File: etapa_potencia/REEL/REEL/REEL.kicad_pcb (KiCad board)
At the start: 2 copper layers, 91.4 x 50.8 mm, 39 parts, among them J1 Conn_display2, J2 Conn_display_2, J3 Conn_teclado, J4 Conn_audio, J5 USB_B_Mini, SW1 SW_Push, SW2 SW_Reed, SW4 BW, SW5 FW, U2 ESP32-WROOM-32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

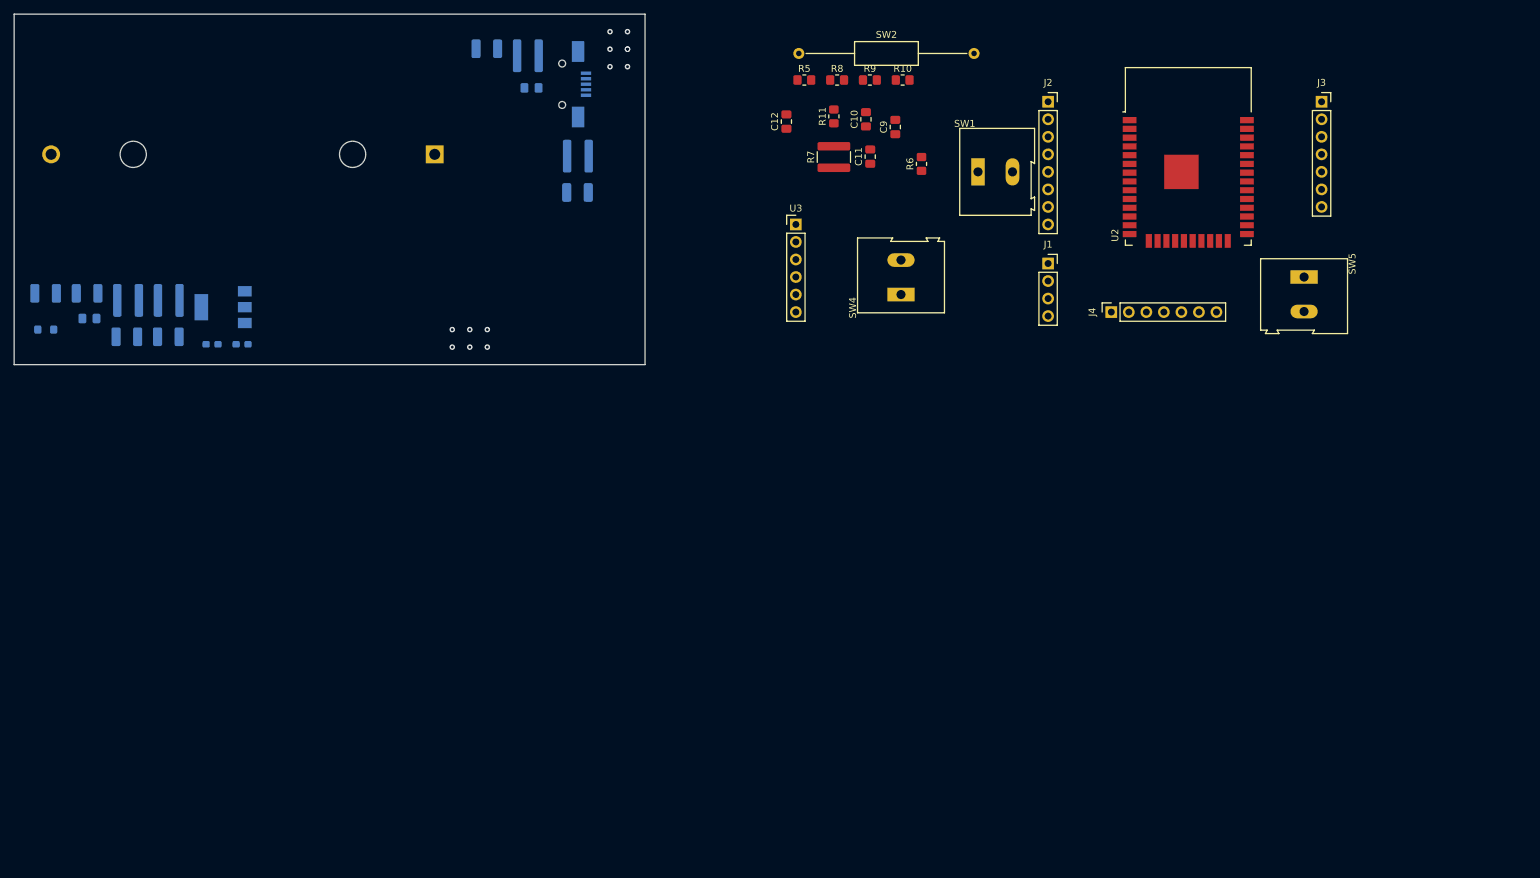
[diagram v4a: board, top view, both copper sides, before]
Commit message: Cambios en diagrama, separacion tierras, y capacitores
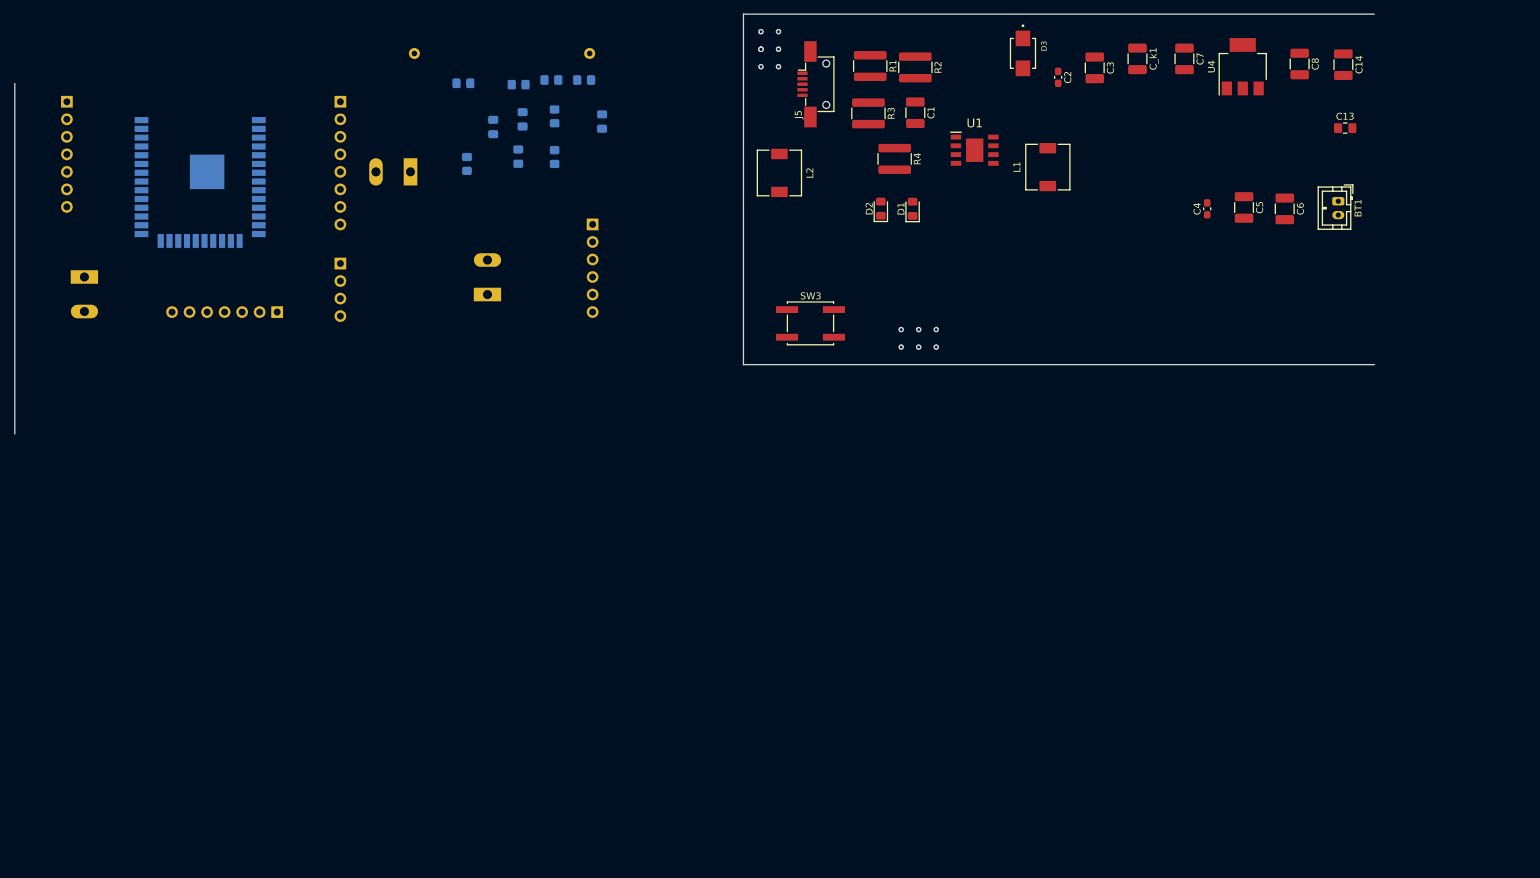
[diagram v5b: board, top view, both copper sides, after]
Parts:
- added C13: 100n, Capacitor_SMD:C_0805_2012Metric_Pad1.18x1.45mm_HandSolder, F.Cu at (210.7, 34.3)
- added C14: 10u, Capacitor_SMD:C_1210_3225Metric_Pad1.33x2.70mm_HandSolder, F.Cu at (210.4, 25.1)
- added C_k1: 10u, Capacitor_SMD:C_1210_3225Metric_Pad1.33x2.70mm_HandSolder, F.Cu at (180.6, 24.3)
- added D3: SMBJ5383B, SMBJ5383B:SMBJ5383B, F.Cu at (164.0, 23.5)
- added L2: 33u, Inductor_SMD:L_6.3x6.3_H3, F.Cu at (128.7, 40.8)
- added SW3: SW_Push, Button_Switch_SMD:SW_SPST_EVQQ2, F.Cu at (133.2, 62.6)
- added U1: Tp5400, KiCad:TP5410, F.Cu at (157.0, 37.5)
- BT1: footprint Battery:BatteryHolder_Bulgin_BX0036_1xC -> Connector_JST:JST_PH_B2B-PH-K_1x02_P2.00mm_Vertical; moved to F.Cu
- C1, C2, C3, C4, C5, C6, D1, D2, J5, R1, R2, R3, R4, U4: moved to F.Cu
- C10, C11, C12, C9, J1, J2, J3, J4, R10, R11, R5, R6, R8, R9, SW1, SW2, SW4, SW5, U2, U3: moved to B.Cu
- C7, C8: value 10u -> 22u; moved to F.Cu
- L1: footprint Inductor_SMD:L_0805_2012Metric_Pad1.05x1.20mm_HandSolder -> Inductor_SMD:L_6.3x6.3_H3; moved to F.Cu
- R7: footprint Resistor_SMD:R_1218_3246Metric_Pad1.22x4.75mm_HandSolder -> Resistor_SMD:R_0805_2012Metric_Pad1.20x1.40mm_HandSolder; moved to B.Cu
- moved J3 181.9 mm to (25.4, 30.5), turned to 180 degrees
- moved C8 178.9 mm to (204.1, 25.0), turned to -90 degrees
- moved SW5 176.8 mm to (28.0, 55.9)
- moved C5 174.1 mm to (196.0, 45.8), turned to -90 degrees
- moved C6 168.8 mm to (201.9, 46.0), turned to -90 degrees
- moved C7 152.7 mm to (187.4, 24.3), turned to -90 degrees
- moved U4 151.8 mm to (195.8, 25.4), turned to 90 degrees
- moved L1 147.1 mm to (167.6, 40.0), turned to 90 degrees
- moved U2 143.2 mm to (44.7, 41.4), turned to 180 degrees
- moved C4 141.3 mm to (190.7, 46.0), turned to 90 degrees
- moved BT1 131.1 mm to (209.7, 44.9), turned to -90 degrees
- moved C2 128.6 mm to (169.1, 26.9), turned to -90 degrees
- moved J4 120.9 mm to (55.9, 61.0)
- moved D1 120.4 mm to (148.0, 46.0), turned to 90 degrees
- moved R2 113.4 mm to (148.4, 25.5), turned to -90 degrees
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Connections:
- J5 pad 1: +5V -> /Power/5V_USB
- J5 pad 6: GND -> Net-(J5-Pad6)
- R1 pad 1: +5V -> /Power/5V_USB
- R2 pad 1: +5V -> /Power/5V_USB
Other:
- board size 91.4 x 50.8 mm -> 197.1 x 60.8 mm

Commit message: modificaciones por caras
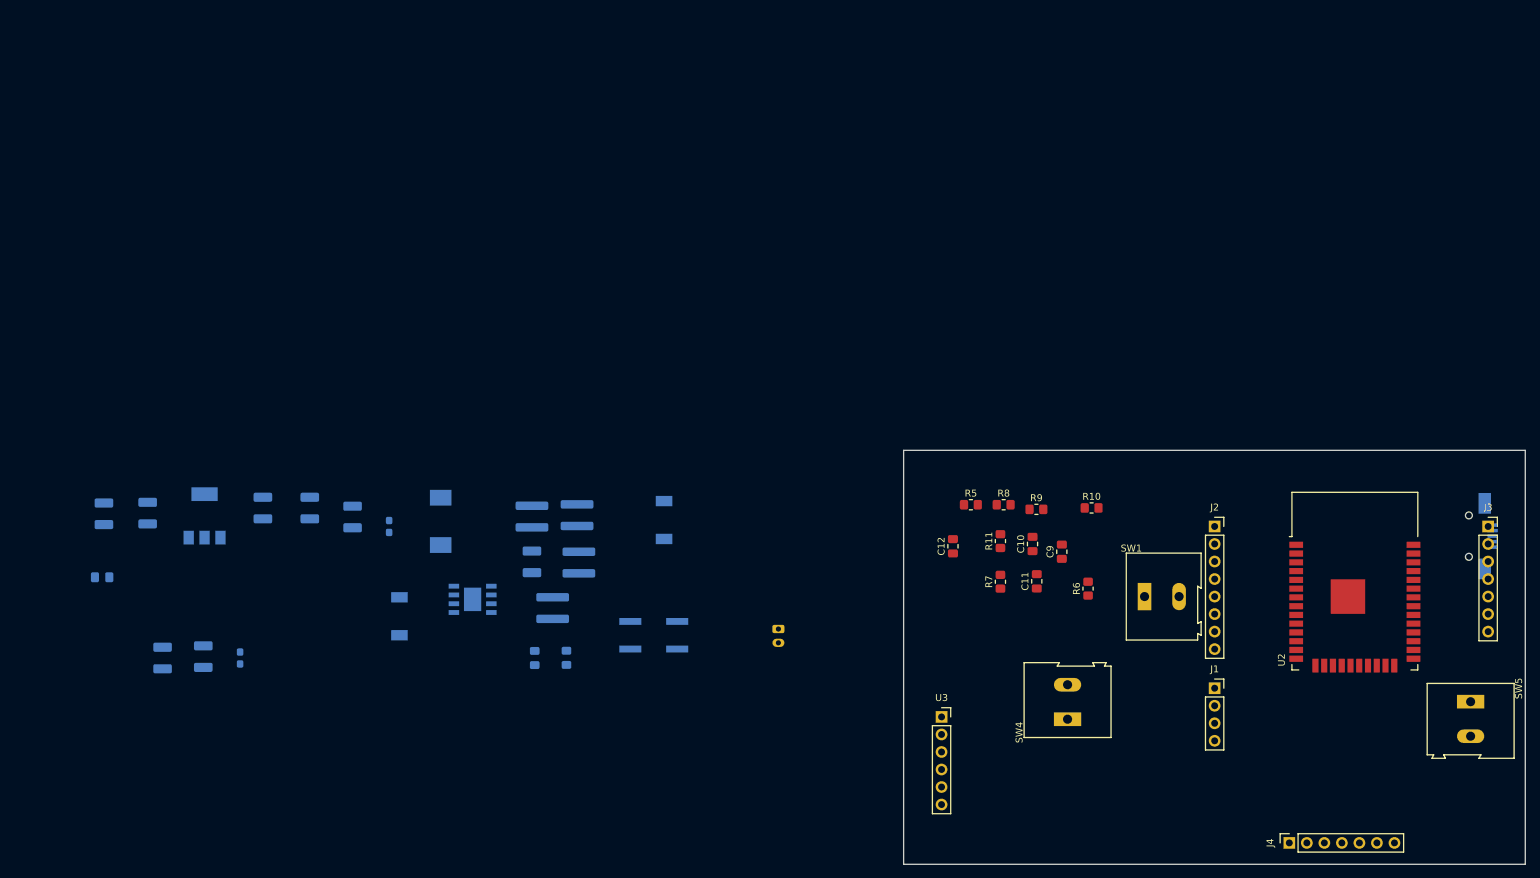
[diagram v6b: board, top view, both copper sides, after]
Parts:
- removed SW2: SW_Reed, Resistor_THT:R_Axial_DIN0309_L9.0mm_D3.2mm_P25.40mm_Horizontal
- BT1, C1, C13, C14, C2, C3, C4, C5, C6, C7, C8, C_k1, D1, D2, J5, L1, L2, R1, R2, R3, R4, SW3, U1, U4: moved to B.Cu
- C10, C11, C12, C9, J1, J2, J3, J4, R10, R11, R5, R6, R7, R8, R9, SW1, SW4, SW5, U2: moved to F.Cu
- D3: value SMBJ5383B -> SS32; footprint SMBJ5383B:SMBJ5383B -> SS32:SS32; moved to B.Cu
- U3: footprint Connector_PinHeader_2.54mm:PinHeader_1x06_P2.54mm_Vertical -> Connector_PinSocket_2.54mm:PinSocket_1x06_P2.54mm_Vertical; moved to F.Cu
- moved J3 215.0 mm to (231.4, 92.0), turned to 0 degrees
- moved SW5 210.1 mm to (228.9, 117.4)
- moved C13 191.6 mm to (30.5, 99.4), turned to 180 degrees
- moved C14 191.1 mm to (30.8, 90.2)
- moved C8 179.2 mm to (37.1, 90.1)
- moved U2 178.3 mm to (212.1, 103.0), turned to 0 degrees
- moved C6 175.2 mm to (39.3, 111.1)
- moved J4 165.6 mm to (202.6, 137.9)
- moved C5 164.3 mm to (45.2, 110.9)
- moved U4 163.9 mm to (45.4, 90.5)
- moved C4 154.5 mm to (50.5, 111.1)
- moved C7 148.6 mm to (53.8, 89.4)
- moved J1 140.9 mm to (191.8, 115.5), turned to 0 degrees
- moved J2 140.9 mm to (191.8, 92.0), turned to 0 degrees
- moved C_k1 136.5 mm to (60.6, 89.4)
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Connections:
- D3 pad A: (no net) -> +5V
- D3 pad C: (no net) -> +5V
- U2 pad 16: Net-(SW2-Pad2) -> unconnected-(U2-Pad16)
- U3 pad 1: (no net) -> unconnected-(U3-Pad1)
- U3 pad 2: (no net) -> /TX_D0
- U3 pad 3: (no net) -> /RX_D0
- U3 pad 4: (no net) -> unconnected-(U3-Pad4)
- U3 pad 5: (no net) -> unconnected-(U3-Pad5)
- U3 pad 6: (no net) -> GND
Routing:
- net (no net): vias 13 -> 0
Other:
- board size 197.1 x 60.8 mm -> 90.1 x 60 mm
- board text removed: "Parte posterior"
- board text removed: "Parte superior"

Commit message: etapa_audio
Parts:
- added J6: Salida_audio, Connector_PinSocket_2.54mm:PinSocket_1x02_P2.54mm_Vertical, F.Cu at (209.6, 125.0)
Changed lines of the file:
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@@
   (net 53 "unconnected-(U3-Pad4)")
   (net 54 "unconnected-(U3-Pad5)")
+  (net 55 "unconnected-(J6-Pad1)")
+  (net 56 "unconnected-(J6-Pad2)")
   (footprint "Capacitor_SMD:C_0805_2012Metric_Pad1.18x1.45mm_HandSolder" (layer "F.Cu")
     (at 169.63 95.695 90)
@@
       (net 48 "/T7") (pinfunction "Pin_7") (pintype "passive"))
     (model "${KICAD6_3DMODEL_DIR}/Connector_PinSocket_2.54mm.3dshapes/PinSocket_1x07_P2.54mm_Vertical.wrl"
+      (offset (xyz 0 0 0))
+      (scale (xyz 1 1 1))
+      (rotate (xyz 0 0 0))
+    )
+  )
+  (footprint "Connector_PinSocket_2.54mm:PinSocket_1x02_P2.54mm_Vertical" (layer "F.Cu")
+    (at 209.55 124.968 90)
+    (descr "Through hole straight socket strip, 1x02, 2.54mm pitch, single row (from Kicad 4.0.7), script generated")
+    (tags "Through hole socket strip THT 1x02 2.54mm single row")
+    (property "Sheetfile" "REEL.kicad_sch")
+    (property "Sheetname" "")
+    (attr through_hole)
+    (fp_text reference "J6" (at 0 -4.064 90) (layer "F.SilkS")
+      (effects (font (size 1 1) (thickness 0.15)))
+    )
+    (fp_text value "Salida_audio" (at 0 5.31 90) (layer "F.Fab")
+      (effects (font (size 1 1) (thickness 0.15)))
+    )
+    (fp_text user "${REFERENCE}" (at 0 1.27) (layer "F.Fab")
+      (effects (font (size 1 1) (thickness 0.15)))
+    )
+    (fp_line (start 1.33 1.27) (end 1.33 3.87) (layer "F.SilkS") (width 0.12))
+    (fp_line (start -1.33 3.87) (end 1.33 3.87) (layer "F.SilkS") (width 0.12))
+    (fp_line (start -1.33 1.27) (end -1.33 3.87) (layer "F.SilkS") (width 0.12))
+    (fp_line (start -1.33 1.27) (end 1.33 1.27) (layer "F.SilkS") (width 0.12))
+    (fp_line (start -1.775 -3.048) (end 1.775 -3.048) (layer "F.CrtYd") (width 0.05))
+    (fp_line (start 1.75 4.3) (end -1.8 4.3) (layer "F.CrtYd") (width 0.05))
+    (fp_line (start -1.8 4.3) (end -1.775 -3.048) (layer "F.CrtYd") (width 0.05))
+    (fp_line (start 1.775 -3.048) (end 1.75 4.3) (layer "F.CrtYd") (width 0.05))
+    (fp_line (start 1.27 3.81) (end -1.27 3.81) (layer "F.Fab") (width 0.1))
+    (fp_line (start -1.27 3.81) (end -1.27 -2.54) (layer "F.Fab") (width 0.1))
+    (fp_line (start 1.3335 -1.7145) (end 1.27 3.81) (layer "F.Fab") (width 0.1))
+    (fp_line (start 0.635 -2.54) (end 1.3335 -1.7145) (layer "F.Fab") (width 0.1))
+    (fp_line (start -1.27 -2.54) (end 0.635 -2.54) (layer "F.Fab") (width 0.1))
+    (pad "1" thru_hole rect (at 0 -1.27 90) (size 1.7 1.7) (drill 1) (layers *.Cu *.Mask)
+      (net 55 "unconnected-(J6-Pad1)") (pinfunction "Pin_1") (pintype "passive+no_connect"))
+    (pad "2" thru_hole oval (at 0 2.54 90) (size 1.7 1.7) (drill 1) (layers *.Cu *.Mask)
+      (net 56 "unconnected-(J6-Pad2)") (pinfunction "Pin_2") (pintype "passive+no_connect"))
+    (model "${KICAD6_3DMODEL_DIR}/Connector_PinSocket_2.54mm.3dshapes/PinSocket_1x02_P2.54mm_Vertical.wrl"
       (offset (xyz 0 0 0))
       (scale (xyz 1 1 1))
@@
     )
   )
+  (gr_line (start 210.185 124.968) (end 210.439 124.968) (layer "Dwgs.User") (width 0.15))
   (gr_rect (start 146.7 81) (end 236.8 141) (layer "Edge.Cuts") (width 0.1) (fill none))
 )

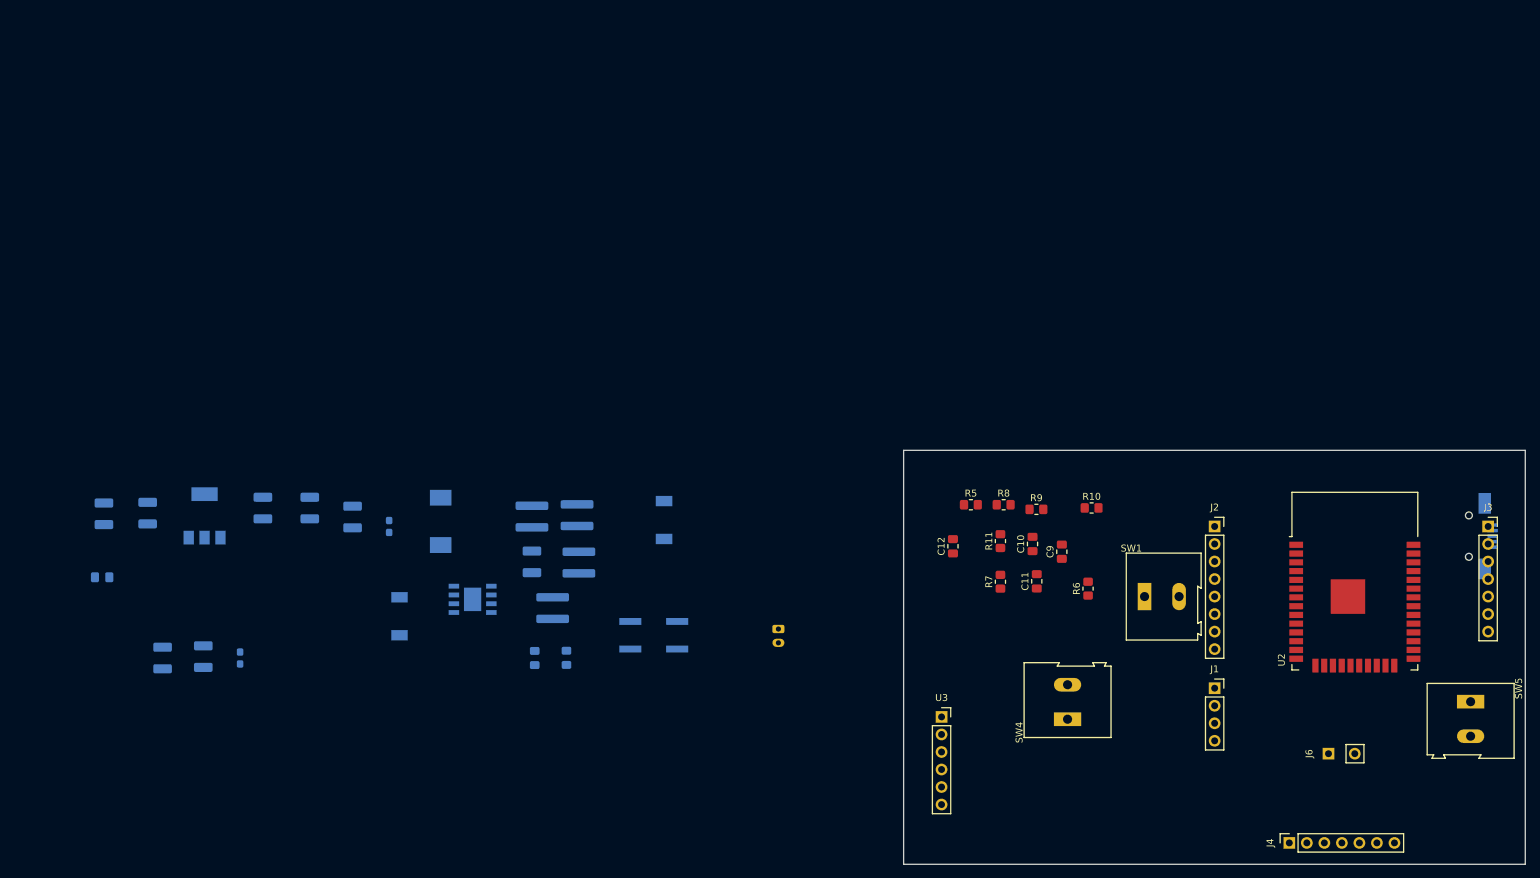
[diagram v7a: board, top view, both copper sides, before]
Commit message: Ubicación definida de los elementos
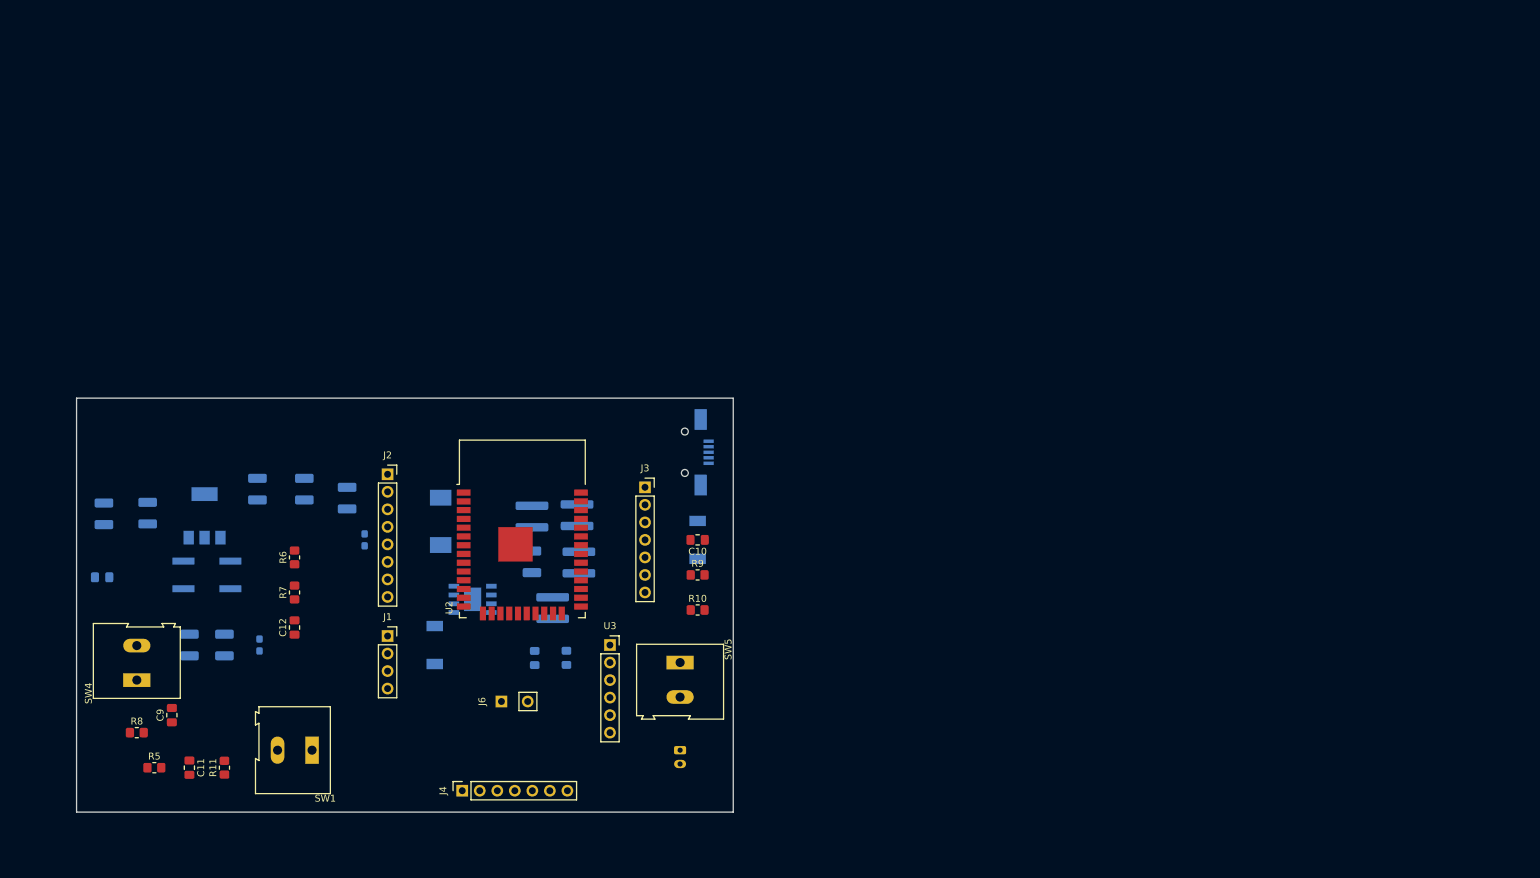
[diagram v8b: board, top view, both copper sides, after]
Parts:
- moved SW4 135.0 mm to (35.6, 114.3)
- moved C9 131.1 mm to (40.6, 119.4)
- moved R8 129.9 mm to (35.6, 121.9)
- moved C11 125.8 mm to (43.2, 127.0), turned to -90 degrees
- moved R5 124.3 mm to (38.1, 127.0)
- moved SW1 122.7 mm to (61.0, 124.5), turned to 180 degrees
- moved J3 122.3 mm to (109.2, 86.4)
- moved U2 120.9 mm to (91.4, 95.4)
- moved J1 120.1 mm to (71.9, 107.9)
- moved J2 120.1 mm to (71.9, 84.5)
- moved J6 120.1 mm to (89.7, 117.4)
- moved J4 120.1 mm to (82.7, 130.3)
- moved R11 117.2 mm to (48.3, 127.0)
- moved R6 115.1 mm to (58.4, 96.5)
- moved SW5 114.7 mm to (114.3, 111.8)
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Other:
- board size 90.1 x 60 mm -> 95.2 x 60 mm
